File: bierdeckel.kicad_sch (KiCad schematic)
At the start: 15 parts, among them J1 Pogo, J2 Pogo, J3 Pogo, J4 Pogo, SW1 Address Coding, SW2 PTS526 SK15 SMTR2 LFS, SW3 PTS526 SK15 SMTR2 LFS, U1 ESP32-C3-WROOM-02

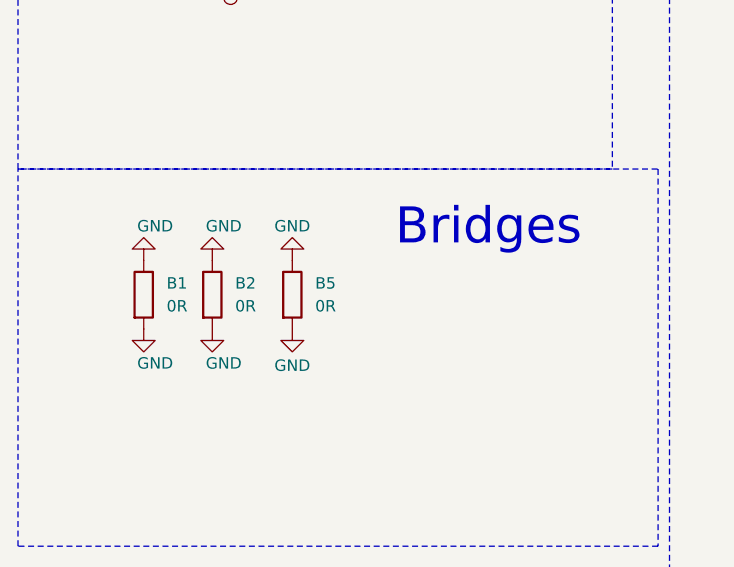
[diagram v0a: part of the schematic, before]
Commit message: reannotate components and move some designators
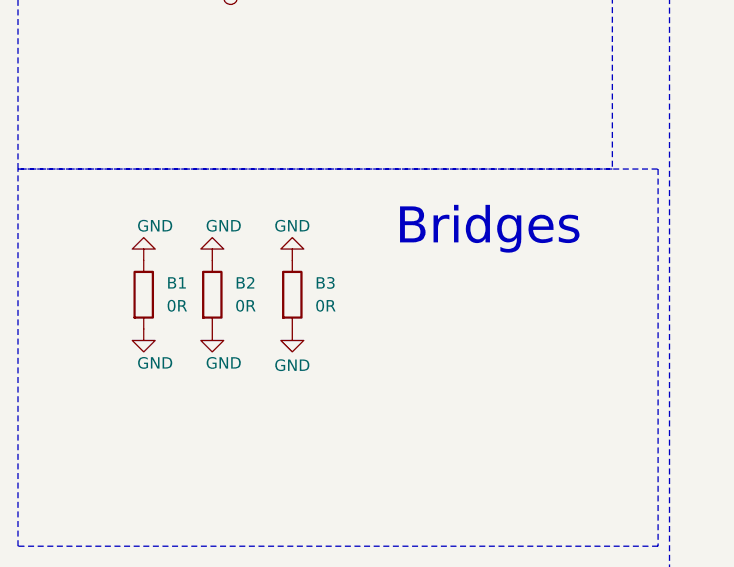
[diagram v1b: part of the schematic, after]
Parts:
- renumbered B5 to B3
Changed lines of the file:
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@@
 		(on_board yes)
 		(dnp no)
-		(property "Reference" "#PWR019"
+		(property "Reference" "#PWR016"
 			(at 215.9 59.69 0)
 			(effects
@@
 			(project "bierdeckel"
 				(path "/a4ffe097-37ef-4e19-a91a-ae57f4a5aad1"
-					(reference "#PWR019")
+					(reference "#PWR016")
 					(unit 1)
 				)
@@
 		(on_board yes)
 		(dnp no)
-		(property "Reference" "#PWR013"
+		(property "Reference" "#PWR07"
 			(at 45.72 85.09 0)
 			(effects
@@
 			(project "bierdeckel"
 				(path "/a4ffe097-37ef-4e19-a91a-ae57f4a5aad1"
-					(reference "#PWR013")
+					(reference "#PWR07")
 					(unit 1)
 				)
@@
 		(on_board yes)
 		(dnp no)
-		(property "Reference" "#PWR012"
+		(property "Reference" "#PWR06"
 			(at 45.72 64.77 0)
 			(effects
@@
 			(project "bierdeckel"
 				(path "/a4ffe097-37ef-4e19-a91a-ae57f4a5aad1"
-					(reference "#PWR012")
+					(reference "#PWR06")
 					(unit 1)
 				)
@@
 		(dnp no)
 		(fields_autoplaced yes)
-		(property "Reference" "#PWR018"
+		(property "Reference" "#PWR015"
 			(at 201.93 106.68 0)
 			(effects
@@
 			(project "bierdeckel"
 				(path "/a4ffe097-37ef-4e19-a91a-ae57f4a5aad1"
-					(reference "#PWR018")
+					(reference "#PWR015")
 					(unit 1)
 				)
@@
 		(dnp no)
 		(fields_autoplaced yes)
-		(property "Reference" "#PWR014"
+		(property "Reference" "#PWR010"
 			(at 156.21 76.2 0)
 			(effects
@@
 			(project "bierdeckel"
 				(path "/a4ffe097-37ef-4e19-a91a-ae57f4a5aad1"
-					(reference "#PWR014")
+					(reference "#PWR010")
 					(unit 1)
 				)
@@
 		(dnp no)
 		(fields_autoplaced yes)
-		(property "Reference" "#PWR015"
+		(property "Reference" "#PWR012"
 			(at 163.83 50.8 0)
 			(effects
@@
 			(project "bierdeckel"
 				(path "/a4ffe097-37ef-4e19-a91a-ae57f4a5aad1"
-					(reference "#PWR015")
+					(reference "#PWR012")
 					(unit 1)
 				)
@@
 		(dnp no)
 		(fields_autoplaced yes)
-		(property "Reference" "#PWR035"
+		(property "Reference" "#PWR011"
 			(at 158.75 107.95 0)
 			(effects
@@
 			(project "bierdeckel"
 				(path "/a4ffe097-37ef-4e19-a91a-ae57f4a5aad1"
-					(reference "#PWR035")
+					(reference "#PWR011")
 					(unit 1)
 				)
@@
 		(dnp no)
 		(fields_autoplaced yes)
-		(property "Reference" "B5"
+		(property "Reference" "B3"
 			(at 48.26 73.66 0)
 			(effects
@@
 			(project "bierdeckel"
 				(path "/a4ffe097-37ef-4e19-a91a-ae57f4a5aad1"
-					(reference "B5")
+					(reference "B3")
 					(unit 1)
 				)
@@
 		(on_board yes)
 		(dnp no)
-		(property "Reference" "#PWR017"
+		(property "Reference" "#PWR014"
 			(at 201.93 48.26 0)
 			(effects
@@
 			(project "bierdeckel"
 				(path "/a4ffe097-37ef-4e19-a91a-ae57f4a5aad1"
-					(reference "#PWR017")
+					(reference "#PWR014")
 					(unit 1)
 				)
@@
 		(dnp no)
 		(fields_autoplaced yes)
-		(property "Reference" "#PWR016"
+		(property "Reference" "#PWR013"
 			(at 163.83 74.93 0)
 			(effects
@@
 			(project "bierdeckel"
 				(path "/a4ffe097-37ef-4e19-a91a-ae57f4a5aad1"
-					(reference "#PWR016")
-					(unit 1)
-				)
+					(reference "#PWR013")
+					(unit 1)
+				)

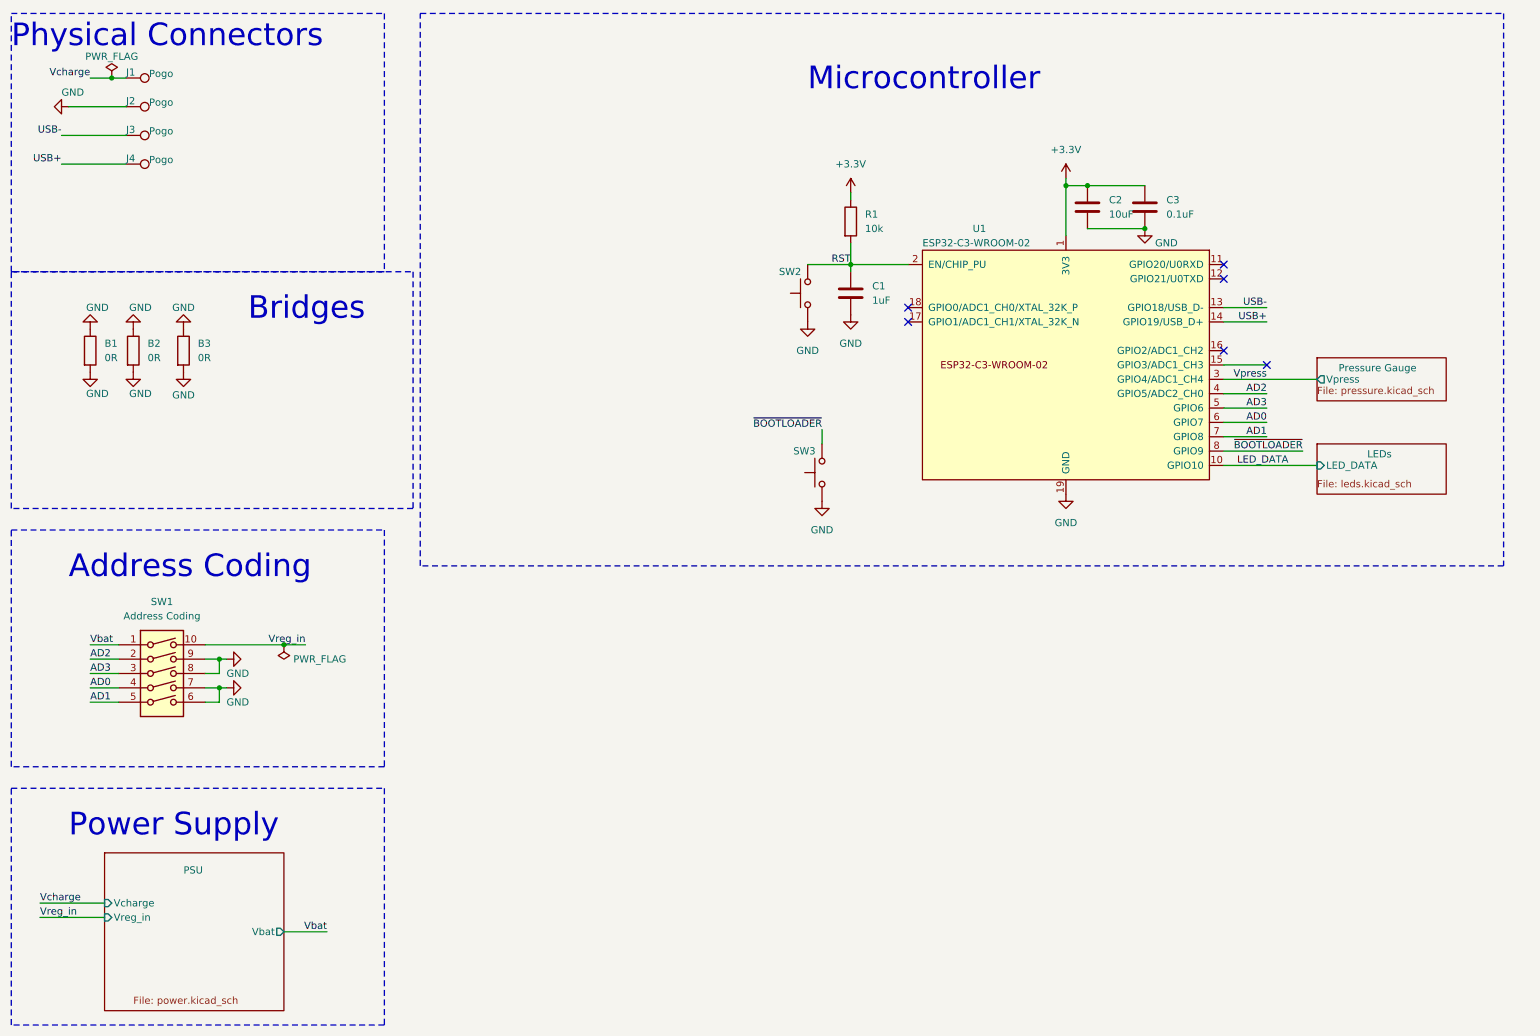
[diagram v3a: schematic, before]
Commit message: implement initial power latching idea
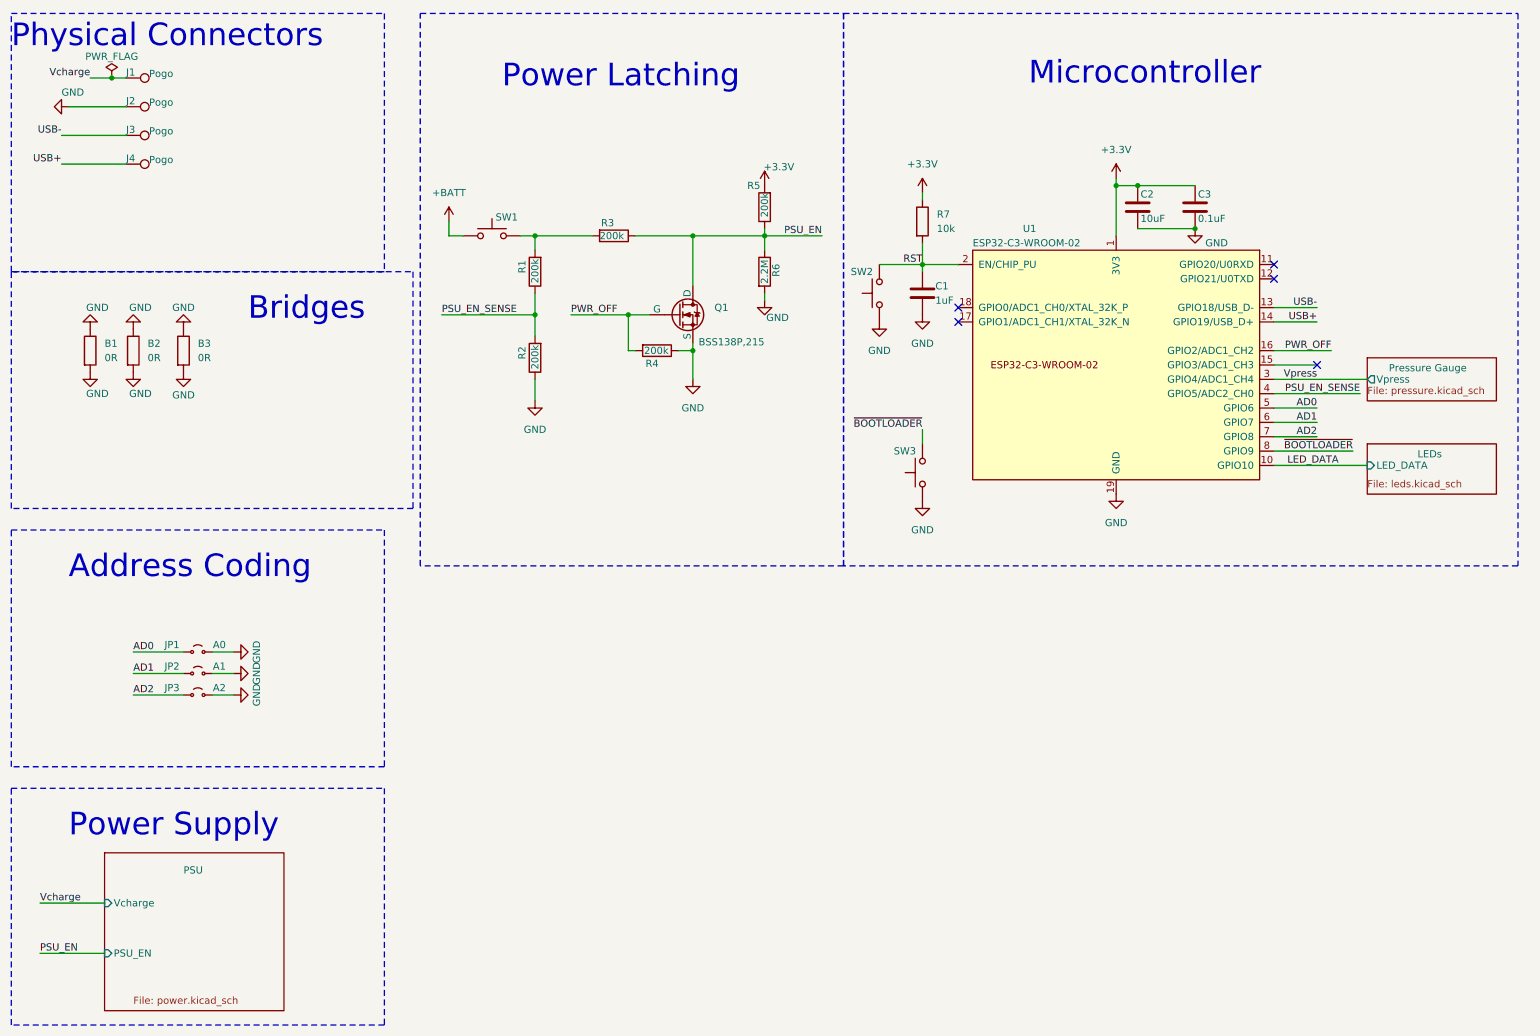
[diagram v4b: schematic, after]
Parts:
- removed SW1: Address Coding, Package_DIP:DIP-10_W8.89mm_SMDSocket_LongPads, symbol bier:SW_DIP_x05
- added JP1: A0, Jumper:SolderJumper-2_P1.3mm_Open_RoundedPad1.0x1.5mm, symbol Jumper:Jumper_2_Small_Open
- added JP2: A1, Jumper:SolderJumper-2_P1.3mm_Open_RoundedPad1.0x1.5mm, symbol Jumper:Jumper_2_Small_Open
- added JP3: A2, Jumper:SolderJumper-2_P1.3mm_Open_RoundedPad1.0x1.5mm, symbol Jumper:Jumper_2_Small_Open
- added Q1: BSS138P,215, Package_TO_SOT_SMD:SOT-23-3, symbol Simulation_SPICE:NMOS
- added R1, R2, R3, R4, R5: 200k, Resistor_SMD:R_0805_2012Metric, symbol Device:R
- added R6: 2.2M, Resistor_SMD:R_0805_2012Metric, symbol Device:R
- added SW1: PTS526 SK15 SMTR2 LFS, Button_Switch_SMD:SW_Push_1P1T_XKB_TS-1187A, symbol Switch:SW_Push
- renumbered R1 to R7
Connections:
- net AD3 is gone; now on net AD0: U1.5 (GPIO6)
- net +3.3V: now also R5.2
- net AD0: now also JP1.1 (A); no longer U1.6 (GPIO7)
- net AD1: now also U1.6 (GPIO7), JP2.1 (A); no longer U1.7 (GPIO8)
- net AD2: now also U1.7 (GPIO8), JP3.1 (A); no longer U1.4 (GPIO5/ADC2_CH0)
- net GND: now also JP1.2 (B), JP2.2 (B), JP3.2 (B), Q1.3 (S), R2.1, R4.1, R6.2
- net PWR_OFF: now reaches U1.16 (GPIO2/ADC1_CH2)
- net PWR_OFF: now also Q1.2 (G), R4.2
- new net: R1.2, R3.2, SW1.2
- new net +BATT: SW1.1
- new net PSU_EN: Q1.1 (D), R3.1, R5.1, R6.1
- new net PSU_EN_SENSE: R1.1, R2.2, U1.4 (GPIO5/ADC2_CH0)
- no-connect marks 6 -> 5
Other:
- sheet PSU ports: added PSU_EN; removed Vbat, Vreg_in
- note added: "Power Latching"
- moved on the sheet: C1, C2, C3, R7, SW2, SW3, U1

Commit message: start reshuffeling for qi-charge version
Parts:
- added B6: 0R, Resistor_SMD:R_1206_3216Metric, symbol Device:R
- J2, J3, J4: footprint TestPoint:TestPoint_Pad_D3.0mm -> TestPoint:TestPoint_Pad_D1.5mm
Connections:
- net GND: now also B6.1, B6.2
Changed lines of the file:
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@@
 			)
 		)
-		(property "Footprint" "TestPoint:TestPoint_Pad_D3.0mm"
+		(property "Footprint" "TestPoint:TestPoint_Pad_D1.5mm"
 			(at 35.56 36.83 0)
 			(effects
@@
 	)
 	(symbol
+		(lib_id "Device:R")
+		(at 53.34 74.93 0)
+		(unit 1)
+		(exclude_from_sim no)
+		(in_bom yes)
+		(on_board yes)
+		(dnp no)
+		(fields_autoplaced yes)
+		(property "Reference" "B6"
+			(at 55.88 73.66 0)
+			(effects
+				(font
+					(size 1.27 1.27)
+				)
+				(justify left)
+			)
+		)
+		(property "Value" "0R"
+			(at 55.88 76.2 0)
+			(effects
+				(font
+					(size 1.27 1.27)
+				)
+				(justify left)
+			)
+		)
+		(property "Footprint" "Resistor_SMD:R_1206_3216Metric"
+			(at 51.562 74.93 90)
+			(effects
+				(font
+					(size 1.27 1.27)
+				)
+				(hide yes)
+			)
+		)
+		(property "Datasheet" "~"
+			(at 53.34 74.93 0)
+			(effects
+				(font
+					(size 1.27 1.27)
+				)
+				(hide yes)
+			)
+		)
+		(property "Description" "Resistor"
+			(at 53.34 74.93 0)
+			(effects
+				(font
+					(size 1.27 1.27)
+				)
+				(hide yes)
+			)
+		)
+		(property "mpn" "CR1206-J/-000ELF"
+			(at 53.34 74.93 0)
+			(effects
+				(font
+					(size 1.27 1.27)
+				)
+				(hide yes)
+			)
+		)
+		(pin "1"
+		)
+		(pin "2"
+		)
+		(instances
+			(project "bierdeckel"
+				(path "/a4ffe097-37ef-4e19-a91a-ae57f4a5aad1"
+					(reference "B6")
+					(unit 1)
+				)
+			)
+		)
+	)
+	(symbol
 		(lib_id "Switch:SW_Push")
 		(at 168.91 64.77 90)
@@
 	)
 	(symbol
+		(lib_id "power:GND")
+		(at 53.34 71.12 180)
+		(unit 1)
+		(exclude_from_sim no)
+		(in_bom yes)
+		(on_board yes)
+		(dnp no)
+		(property "Reference" "#PWR071"
+			(at 53.34 64.77 0)
+			(effects
+				(font
+					(size 1.27 1.27)
+				)
+				(hide yes)
+			)
+		)
+		(property "Value" "GND"
+			(at 53.34 67.31 0)
+			(effects
+				(font
+					(size 1.27 1.27)
+				)
+			)
+		)
+		(property "Footprint" ""
+			(at 53.34 71.12 0)
+			(effects
+				(font
+					(size 1.27 1.27)
+				)
+				(hide yes)
+			)
+		)
+		(property "Datasheet" ""
+			(at 53.34 71.12 0)
+			(effects
+				(font
+					(size 1.27 1.27)
+				)
+				(hide yes)
+			)
+		)
+		(property "Description" "Power symbol creates a global label with name \"GND\" , ground"
+			(at 53.34 71.12 0)
+			(effects
+				(font
+					(size 1.27 1.27)
+				)
+				(hide yes)
+			)
+		)
+		(pin "1"
+		)
+		(instances
+			(project "bierdeckel"
+				(path "/a4ffe097-37ef-4e19-a91a-ae57f4a5aad1"
+					(reference "#PWR071")
+					(unit 1)
+				)
+			)
+		)
+	)
+	(symbol
 		(lib_id "Connector:TestPoint")
 		(at 35.56 26.67 270)
@@
 	(symbol
 		(lib_id "power:GND")
+		(at 53.34 78.74 0)
+		(unit 1)
+		(exclude_from_sim no)
+		(in_bom yes)
+		(on_board yes)
+		(dnp no)
+		(property "Reference" "#PWR072"
+			(at 53.34 85.09 0)
+			(effects
+				(font
+					(size 1.27 1.27)
+				)
+				(hide yes)
+			)
+		)
+		(property "Value" "GND"
+			(at 53.34 82.804 0)
+			(effects
+				(font
+					(size 1.27 1.27)
+				)
+			)
+		)
+		(property "Footprint" ""
+			(at 53.34 78.74 0)
+			(effects
+				(font
+					(size 1.27 1.27)
+				)
+				(hide yes)
+			)
+		)
+		(property "Datasheet" ""
+			(at 53.34 78.74 0)
+			(effects
+				(font
+					(size 1.27 1.27)
+				)
+				(hide yes)
+			)
+		)
+		(property "Description" "Power symbol creates a global label with name \"GND\" , ground"
+			(at 53.34 78.74 0)
+			(effects
+				(font
+					(size 1.27 1.27)
+				)
+				(hide yes)
+			)
+		)
+		(pin "1"
+		)
+		(instances
+			(project "bierdeckel"
+				(path "/a4ffe097-37ef-4e19-a91a-ae57f4a5aad1"
+					(reference "#PWR072")
+					(unit 1)
+				)
+			)
+		)
+	)
+	(symbol
+		(lib_id "power:GND")
 		(at 148.59 66.04 0)
 		(unit 1)
@@
 			)
 		)
-		(property "Footprint" "TestPoint:TestPoint_Pad_D3.0mm"
+		(property "Footprint" "TestPoint:TestPoint_Pad_D1.5mm"
 			(at 35.56 41.91 0)
 			(effects
@@
 			)
 		)
-		(property "Footprint" "TestPoint:TestPoint_Pad_D3.0mm"
+		(property "Footprint" "TestPoint:TestPoint_Pad_D1.5mm"
 			(at 35.56 46.99 0)
 			(effects

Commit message: continue refactor
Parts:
- added U5: ESP32-C3-MINI-1, PCM_Espressif:ESP32-C3-MINI-1, symbol PCM_Espressif:ESP32-C3-MINI-1
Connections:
- net +3.3V: now also U5.3 (3V3)
- net AD0: now also U5.20 (GPIO6)
- net AD1: now also U5.21 (GPIO7)
- net AD2: now also U5.22 (GPIO8)
- net GND: now also U5.1 (GND), U5.11 (GND), U5.14 (GND), U5.2 (GND), U5.36 (GND), U5.37 (GND), U5.38 (GND), U5.39 (GND), U5.40 (GND), U5.41 (GND), U5.42 (GND), U5.43 (GND), U5.44 (GND), U5.45 (GND), U5.46 (GND), U5.47 (GND), U5.48 (GND), U5.49 (GND), U5.50 (GND), U5.51 (GND), U5.52 (GND), U5.53 (GND)
- net LED_DATA: now also U5.16 (GPIO10)
- net PSU_EN_SENSE: now also U5.19 (GPIO5/ADC2_CH0)
- net PWR_OFF: now also U5.5 (GPIO2/ADC1_CH2)
- net RST: now also U5.8 (EN/CHIP_PU)
- net USB+: now also U5.27 (GPIO19/USB_D+)
- net USB-: now also U5.26 (GPIO18/USB_D-)
- net Vpress: now also U5.18 (GPIO4/ADC1_CH4)
- net ~{BOOTLOADER}: now also U5.23 (GPIO9)
- no-connect marks 5 -> 10

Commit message: further work
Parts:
- C3: footprint Capacitor_SMD:C_0805_2012Metric -> Capacitor_SMD:C_0603_1608Metric
- R1, R2, R3, R4, R5, R6, R7: footprint Resistor_SMD:R_0805_2012Metric -> Resistor_SMD:R_0603_1608Metric
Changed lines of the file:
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@@
 			)
 		)
-		(property "Footprint" "Resistor_SMD:R_0805_2012Metric"
+		(property "Footprint" "Resistor_SMD:R_0603_1608Metric"
 			(at 129.54 73.152 90)
 			(effects
@@
 			)
 		)
-		(property "Footprint" "Capacitor_SMD:C_0805_2012Metric"
+		(property "Footprint" "Capacitor_SMD:C_0603_1608Metric"
 			(at 225.7552 53.34 0)
 			(effects
@@
 			)
 		)
-		(property "Footprint" "Resistor_SMD:R_0805_2012Metric"
+		(property "Footprint" "Resistor_SMD:R_0603_1608Metric"
 			(at 121.92 52.832 90)
 			(effects
@@
 			)
 		)
-		(property "Footprint" "Resistor_SMD:R_0805_2012Metric"
+		(property "Footprint" "Resistor_SMD:R_0603_1608Metric"
 			(at 109.728 76.2 90)
 			(effects
@@
 			)
 		)
-		(property "Footprint" "Resistor_SMD:R_0805_2012Metric"
+		(property "Footprint" "Resistor_SMD:R_0603_1608Metric"
 			(at 109.728 60.96 90)
 			(effects
@@
 			)
 		)
-		(property "Footprint" "Resistor_SMD:R_0805_2012Metric"
+		(property "Footprint" "Resistor_SMD:R_0603_1608Metric"
 			(at 146.812 60.96 90)
 			(effects
@@
 			)
 		)
-		(property "Footprint" "Resistor_SMD:R_0805_2012Metric"
+		(property "Footprint" "Resistor_SMD:R_0603_1608Metric"
 			(at 150.368 49.53 90)
 			(effects
@@
 			)
 		)
-		(property "Footprint" "Resistor_SMD:R_0805_2012Metric"
+		(property "Footprint" "Resistor_SMD:R_0603_1608Metric"
 			(at 174.752 52.07 90)
 			(effects

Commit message: before USB connector
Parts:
- added J6: USB4110-GF-A, Connector_USB:USB_C_Receptacle_GCT_USB4110, symbol Connector:USB_C_Receptacle_USB2.0_16P
- added R23, R24: 5k1, Resistor_SMD:R_0603_1608Metric, symbol Device:R
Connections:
- net GND: now also J6.A1 (GND), J6.A12 (GND), J6.B1 (GND), J6.B12 (GND), J6.S1 (SHIELD), R23.2, R24.2
- net USB+: now also J6.A6 (D+), J6.B6 (D+)
- net USB-: now also J6.A7 (D-), J6.B7 (D-)
- net Vcharge: now also J6.A4 (VBUS), J6.A9 (VBUS), J6.B4 (VBUS), J6.B9 (VBUS)
- new net: J6.A5 (CC1), R23.1
- new net: J6.B5 (CC2), R24.1
- no-connect marks 10 -> 12
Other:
- moved on the sheet: B1, B2, B3, B6, J1, J2, J3, J4
